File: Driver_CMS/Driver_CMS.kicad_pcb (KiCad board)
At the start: 2 copper layers, 47.5 x 30 mm, 25 parts, among them J1 Screw_Terminal_01x04, J2 Screw_Terminal_01x04, J3 Screw_Terminal_01x03, U2 L298HN

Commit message: Driver CMS DRC OK
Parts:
- U2: value L298HN -> L298P
- moved U2 0.54 mm to (153.3, 57.7)
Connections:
- U2 pad 10: alim_bobine3 -> GND
- U2 pad 11: +5V -> GND
- U2 pad 12: alim_bobine4 -> +5V
- U2 pad 13: out_bobine3 -> alim_bobine3
- U2 pad 14: out_bobine4 -> +5V
- U2 pad 15: GND -> alim_bobine4
- U2 pad 16: (no net) -> out_bobine3
- U2 pad 17: (no net) -> out_bobine4
- U2 pad 18: (no net) -> unconnected-(U2-NC-Pad18)
- U2 pad 19: (no net) -> GND
- U2 pad 2: out_bobine1 -> GND
- U2 pad 20: (no net) -> GND
- U2 pad 3: out_bobine2 -> unconnected-(U2-NC-Pad3)
- U2 pad 4: +24V -> out_bobine1
- U2 pad 5: alim_bobine1 -> out_bobine2
- U2 pad 6: +5V -> +24V
- U2 pad 7: alim_bobine2 -> alim_bobine1
- U2 pad 8: GND -> +5V
- U2 pad 9: +5V -> alim_bobine2
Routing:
- net alim_bobine3: track 14.6 -> 39.6 mm
- net +5V: track 92.1 -> 72.8 mm
- net alim_bobine4: track 35.2 -> 44.7 mm
- net out_bobine4: track 54.4 -> 60.7 mm
- net GND: track 11.1 -> 7.58 mm, vias 0 -> 3
- net out_bobine1: track 25.9 -> 28.0 mm
- net out_bobine3: track 53.6 -> 51.5 mm
- net out_bobine2: track 24.2 -> 26.1 mm
- net alim_bobine2: track 16.8 -> 15.4 mm

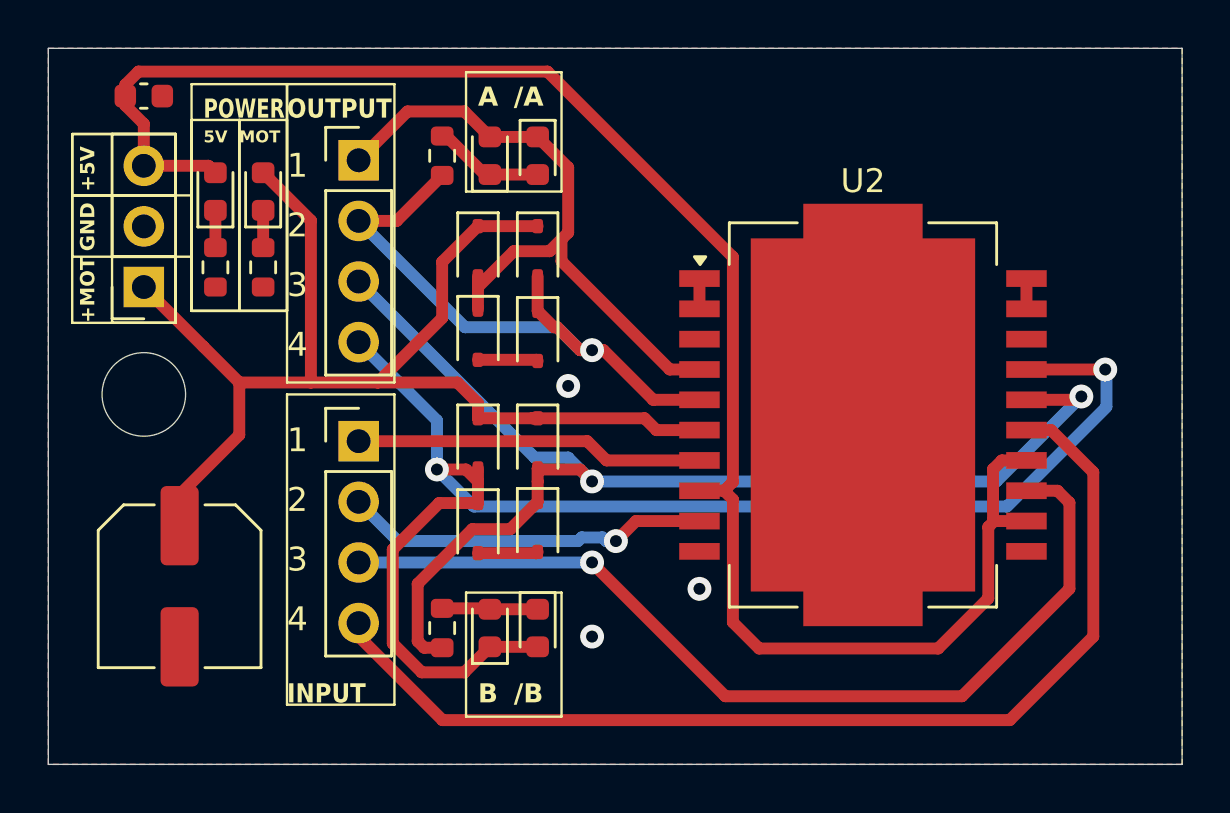
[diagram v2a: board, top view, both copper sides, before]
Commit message: Send Fabraication Files & add DC/DC files
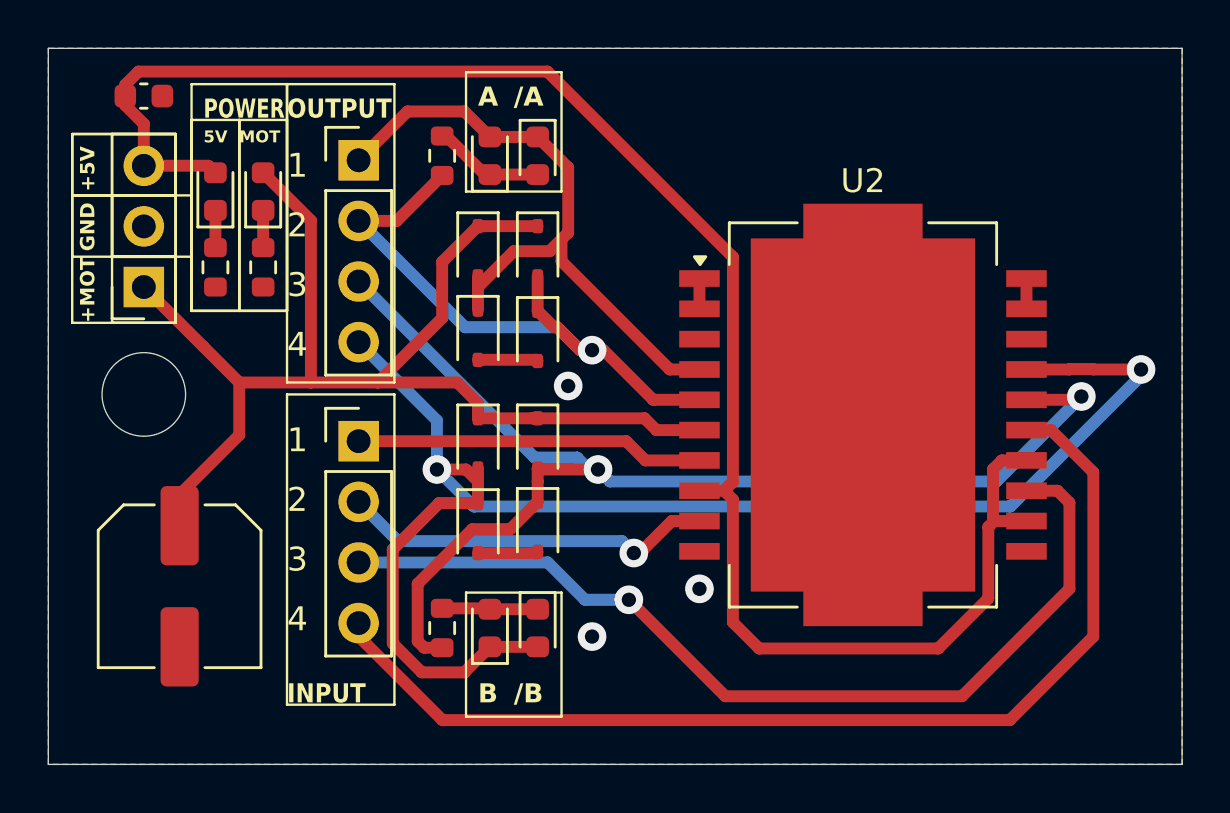
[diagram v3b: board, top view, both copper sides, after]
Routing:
- net out_bobine4: track 60.7 -> 62.9 mm
